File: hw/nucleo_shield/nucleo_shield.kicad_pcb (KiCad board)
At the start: 2 copper layers, 151 x 90.9 mm, 83 parts, among them CN101 Nucleo-F411RE-CN10, CN71 Nucleo-F411RE-CN7, P1 CONN_INH1, P10 CONN_OUTH1, P11 CONN_OUTH2, P12 CONN_RS485_OUT, P13 CONN_RS485_IN, P14 CONN_OUT2, P15 CONN_EXT2, P16 CONN_EXTI2C, P17 CONN_EXT, P18 CONN_1WIRE, P19 CONN_EXT_SPI, P2 CONN_OUT3, P20 CON_BME, P3 CONN_OUT1, P4 POWER_CON, P5 CONN_INH2, P6 ETH_CONN, P7 CONN_LCD_SD, P8 CONN_OUT4, P9 CONN_SCT, U1 74HC595, U10 ULN2803, U11 74HC595, U12 74HC595, U2 74HC595, U3 LTV-847, U4 LTV-847, U5 LTV-847, U6 LTV-847, U7 PCF8574A, U8 PCF8574A, U9 ULN2803

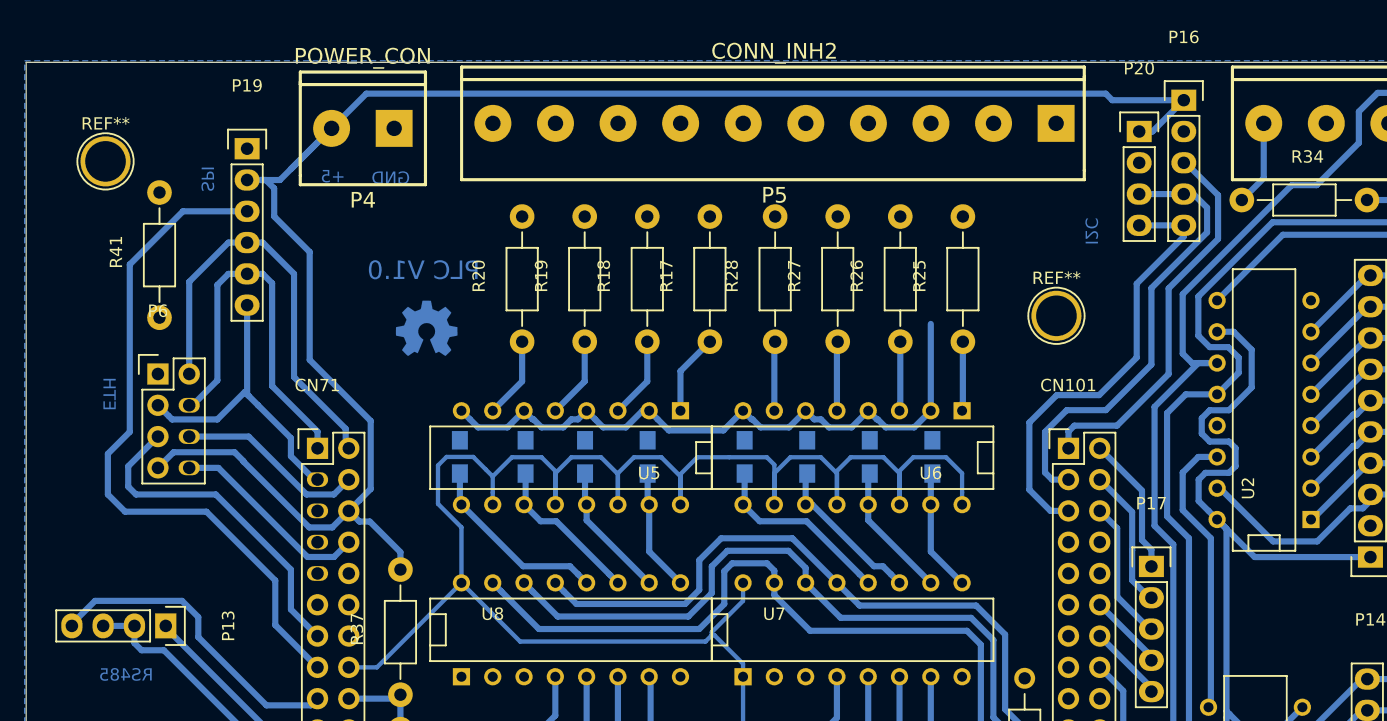
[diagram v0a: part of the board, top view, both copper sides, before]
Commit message: PCB: place connector for BME280
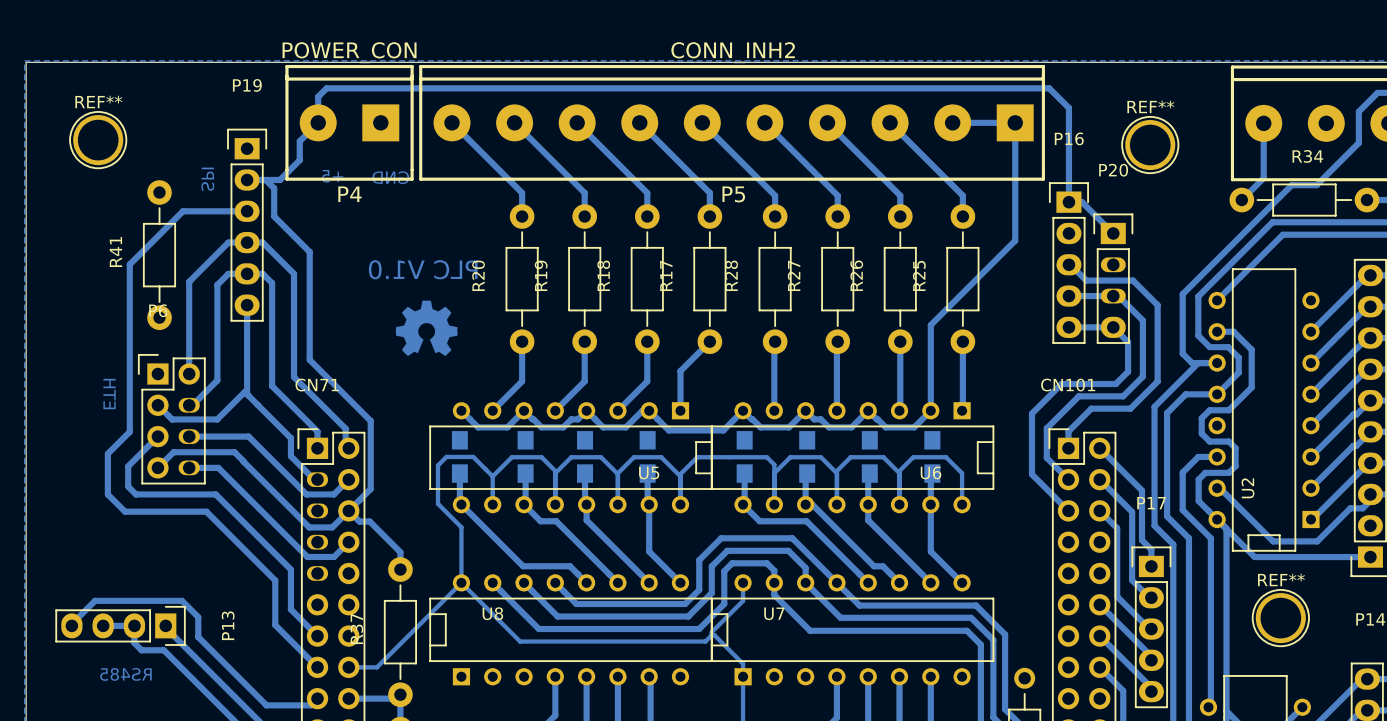
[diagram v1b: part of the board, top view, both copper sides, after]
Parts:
- added REF**: 1pin, Connect:1pin, F.Cu at (197.0, 103.2)
- moved REF** 15.8 mm to (186.4, 64.8)
- moved P16 12.5 mm to (179.8, 69.4)
- moved P20 8.54 mm to (183.4, 71.9)
- moved P5 3.32 mm to (152.5, 63.0)
- moved REF** 1.83 mm to (101.0, 64.4)
- moved P4 1.17 mm to (121.4, 63.0)
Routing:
- net GND_24V: track 129.6 -> 153.8 mm
- net I2C1_SCL: track 37.3 -> 26.2 mm
- net I2C1_SDA: track 36.2 -> 26.1 mm
- net inh16: track 0.00 -> 10.1 mm
- net inh15: track 0.27 -> 10.3 mm
- net inh13: track 0.27 -> 10.3 mm
- net inh14: track 0.00 -> 10.1 mm
- net inh11: track 0.00 -> 9.96 mm
- net inh10: track 0.00 -> 9.96 mm
- net inh9: track 0.04 -> 10.0 mm
- net inh12: track 0.04 -> 10.0 mm
- net I2C_GPIO: track 31.5 -> 25.0 mm
- net +5V: track 536.2 -> 532.6 mm
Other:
- board text removed: "I2C"

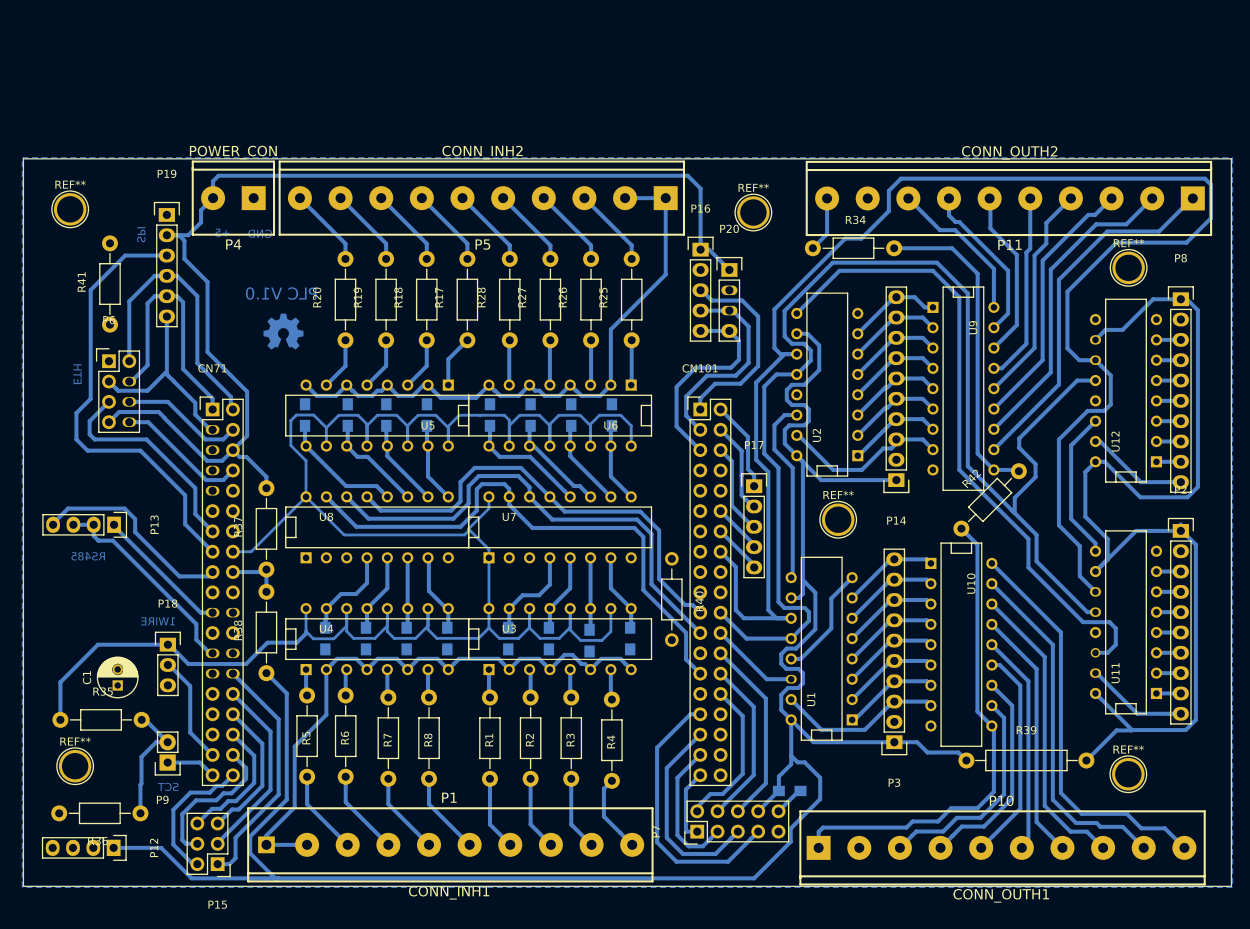
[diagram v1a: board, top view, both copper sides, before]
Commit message: Nucleo: add missing connections
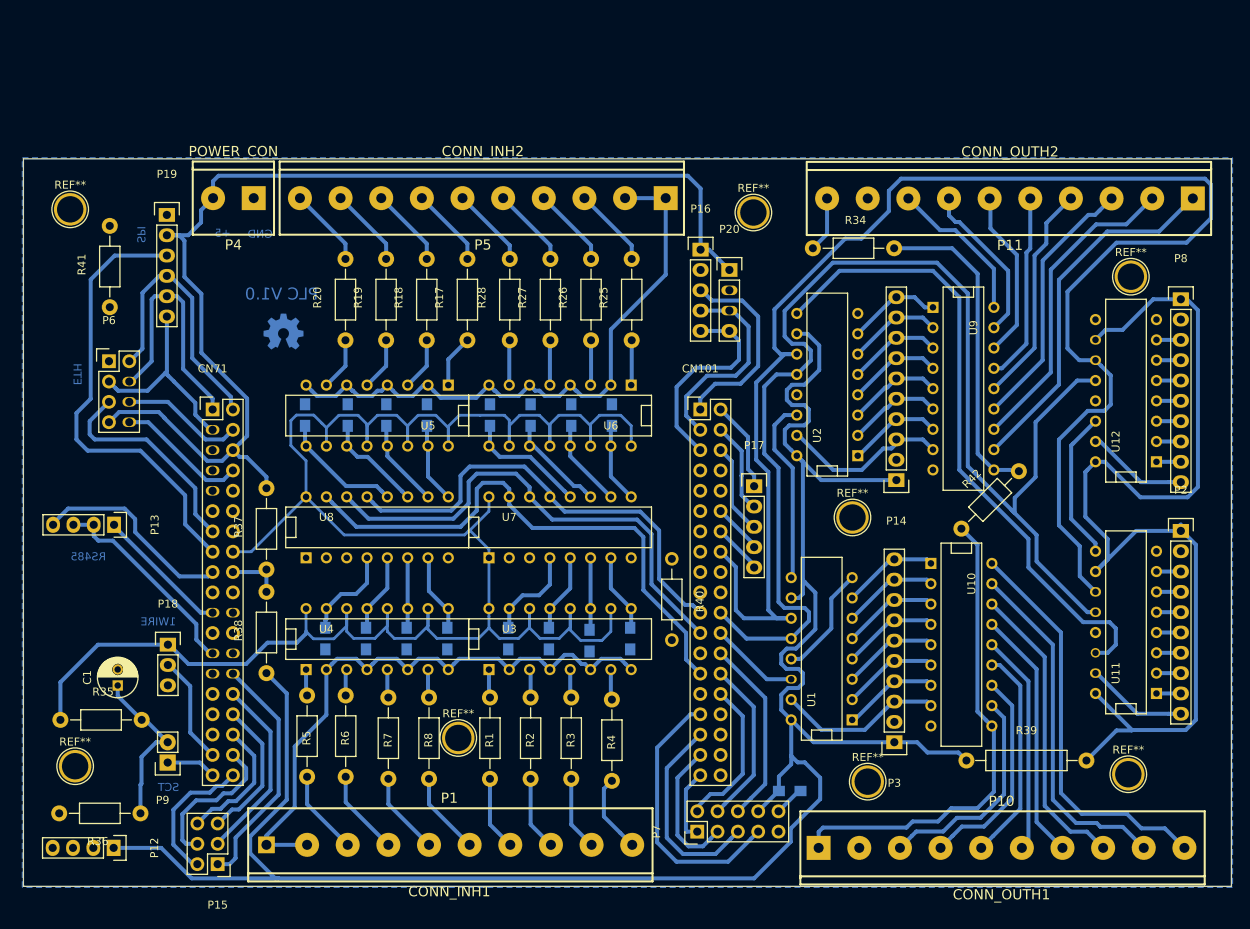
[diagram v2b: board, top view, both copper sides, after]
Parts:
- added REF**: 1pin, Connect:1pin, F.Cu at (198.8, 102.9)
- added REF**: 1pin, Connect:1pin, F.Cu at (149.5, 130.4)
- moved REF** 32.9 mm to (200.7, 135.9)
- moved R41 2.18 mm to (105.9, 71.5)
- moved REF** 1.14 mm to (233.6, 72.8)
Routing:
- net Net-(C1-Pad1): track 15.6 -> 21.1 mm
- net SRLatch: track 160.3 -> 158.6 mm
- net IO_INT: track 57.0 -> 58.0 mm
- net SPI3_MISO: track 34.4 -> 33.6 mm
- net EXT_SPI_SS: track 55.8 -> 56.6 mm
- net I2C3_SCL: track 61.3 -> 61.9 mm

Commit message: Nucleo: update schematic and remove intermediate header for outputs
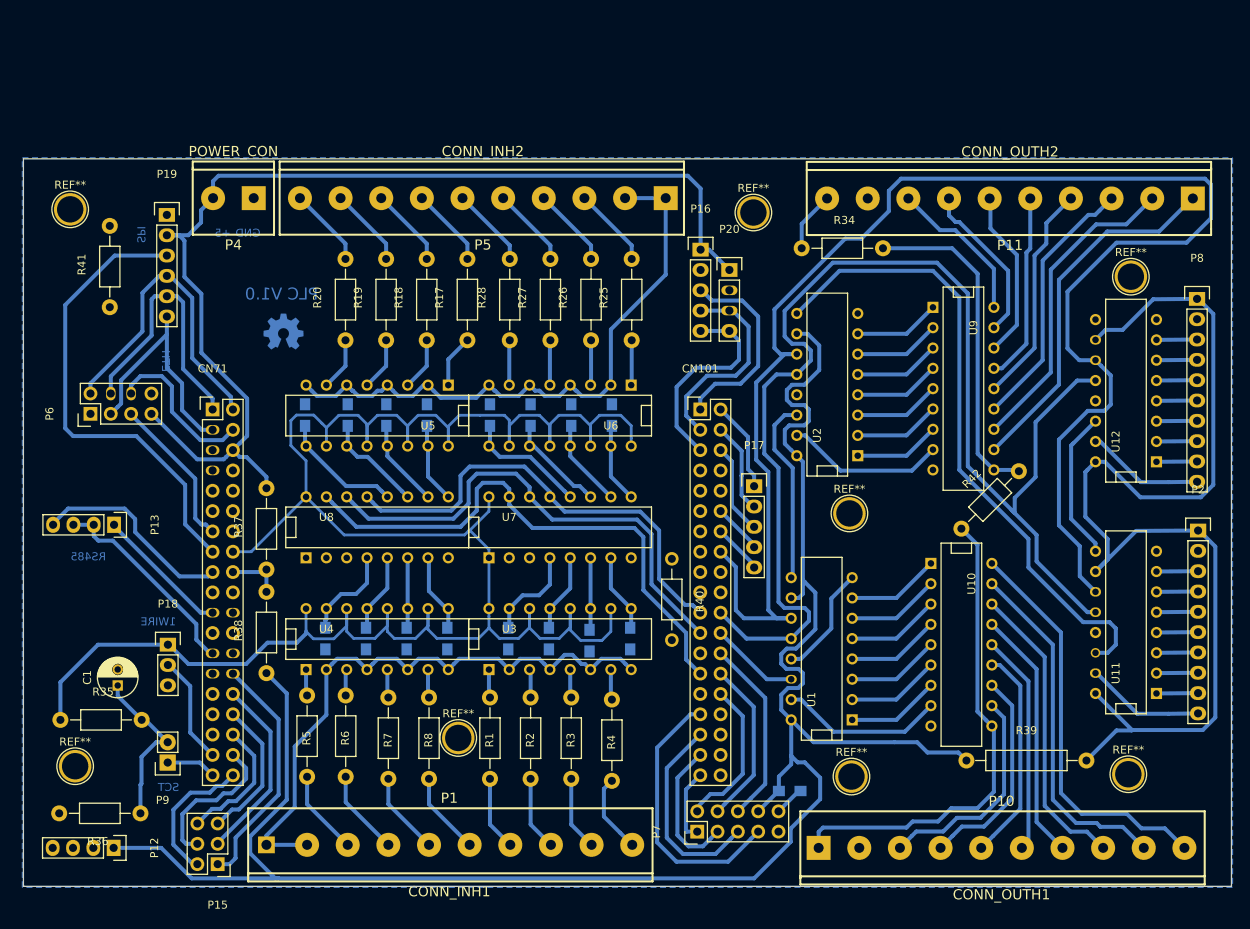
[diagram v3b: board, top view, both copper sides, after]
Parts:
- removed P14: CONN_OUT2, Pin_Headers:Pin_Header_Straight_1x10
- removed P3: CONN_OUT1, Pin_Headers:Pin_Header_Straight_1x10
- moved P6 6.97 mm to (103.5, 89.9), turned to 90 degrees
- moved P2 2.15 mm to (242.0, 104.5)
- moved REF** 2.13 mm to (198.6, 135.3)
- moved P8 2.03 mm to (241.8, 75.5)
- moved R34 1.40 mm to (197.5, 69.2)
- moved REF** 0.64 mm to (198.4, 102.4)
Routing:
- net GND: track 30.7 -> 14.2 mm
- net +5V: track 532.6 -> 520.4 mm
- net ETH_CS: track 27.4 -> 19.2 mm
- net SPI3_MISO: track 33.6 -> 39.6 mm
- net SPI3_MOSI: track 25.7 -> 30.9 mm
- net ETH_RST: track 15.4 -> 19.9 mm
- net SPI3_SCK: track 30.9 -> 33.2 mm
- net out17: track 12.8 -> 14.9 mm
- net out24: track 3.05 -> 5.20 mm
- net out23: track 3.05 -> 5.20 mm
- net out22: track 3.05 -> 5.20 mm
- net out21: track 3.05 -> 5.20 mm
- net out20: track 3.05 -> 5.20 mm
- net out19: track 3.05 -> 5.20 mm
- net out18: track 3.05 -> 5.20 mm
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
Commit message: Nucleo: ad vias
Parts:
- removed G***: LOGO, LOGO
- removed R34, R37, R38, R40, R41, R42: R, Resistors_ThroughHole:Resistor_Horizontal_RM10mm
- removed R39: R, Resistors_ThroughHole:Resistor_Horizontal_RM15mm
- removed the REF** at (198.4, 102.4)
- removed the REF** at (149.5, 130.4)
- removed the REF** at (198.6, 135.3)
- removed the REF** at (186.4, 64.8)
- removed the REF** at (233.6, 72.8)
- removed the REF** at (101.6, 134.0)
- removed the REF** at (233.2, 135.0)
- removed the REF** at (101.0, 64.4)
- added REF**: MountingHole_3mm, Mounting_Holes:MountingHole_3mm, F.Cu at (238.1, 71.8)
- added REF**: MountingHole_3mm, Mounting_Holes:MountingHole_3mm, F.Cu at (238.6, 136.3)
- added REF**: MountingHole_3mm, Mounting_Holes:MountingHole_3mm, F.Cu at (101.9, 64.3)
- added REF**: MountingHole_3mm, Mounting_Holes:MountingHole_3mm, F.Cu at (186.6, 64.5)
- added REF**: MountingHole_3mm, Mounting_Holes:MountingHole_3mm, F.Cu at (200.9, 136.3)
- added REF**: MountingHole_3mm, Mounting_Holes:MountingHole_3mm, F.Cu at (200.4, 102.7)
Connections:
- U9 pad 10: Net-(R34-Pad2) -> +24V
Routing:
- net +24V: track 68.1 -> 123.1 mm, vias 0 -> 4
- net GND: track 14.2 -> 69.1 mm, vias 0 -> 4
- net Net-(R34-Pad2): track 41.7 -> 0.00 mm
- net +5V: track 520.4 -> 555.8 mm, vias 0 -> 6
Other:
- board text removed: "+5"
- board text removed: "1WIRE"
- board text removed: "ETH"
- board text removed: "GND"
- board text removed: "RS485"
- board text removed: "SCT"
- board text removed: "SPI"

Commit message: WIP: add more IO
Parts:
- removed P17: CONN_EXT, Pin_Headers:Pin_Header_Straight_1x05
- removed REF** (x6): MountingHole_3mm, Mounting_Holes:MountingHole_3mm
- added P3: POWER_24V_CON, w_conn_screw:mors_2p, F.Cu at (112.9, 62.7)
- added U14: PCF8574A, Housings_DIP:DIP-16__300, F.Cu at (193.8, 97.9)
- P1, P10, P11, P5: footprint w_conn_screw:mors_10p -> w_conn_screw:mors_8p
- P2, P8: footprint Pin_Headers:Pin_Header_Straight_1x10 -> Pin_Headers:Pin_Header_Straight_1x08
- moved U2 57.2 mm to (235.8, 126.9)
- moved P16 49.2 mm to (225.7, 51.7), turned to 180 degrees
- moved P20 44.3 mm to (221.4, 49.1), turned to 180 degrees
- moved U11 33.9 mm to (220.0, 84.7), turned to 180 degrees
- moved P19 23.7 mm to (100.3, 85.1), turned to 90 degrees
- moved U1 22.9 mm to (217.6, 122.7), turned to 0 degrees
- moved P4 19.9 mm to (101.5, 62.7)
- moved R20 15.8 mm to (119.6, 75.1)
- moved R25 15.8 mm to (155.4, 80.3)
- moved R19 15.8 mm to (124.7, 75.3)
- moved R17 15.8 mm to (134.9, 75.3)
- moved R18 15.8 mm to (129.8, 75.3)
- moved R26 15.8 mm to (150.3, 80.3)
- moved R27 15.8 mm to (145.2, 80.3)
- moved R28 15.8 mm to (140.2, 80.3)
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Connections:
- CN101 pad 10: (no net) -> Net-(CN101-Pad10)
- CN101 pad 11: (no net) -> Net-(CN101-Pad11)
- CN101 pad 12: Net-(CN101-Pad12) -> SRLatch2
- CN101 pad 13: (no net) -> Net-(CN101-Pad13)
- CN101 pad 14: Net-(CN101-Pad14) -> SRDATA2
- CN101 pad 15: (no net) -> Net-(CN101-Pad15)
- CN101 pad 17: (no net) -> Net-(CN101-Pad17)
- CN101 pad 18: (no net) -> Net-(CN101-Pad18)
- CN101 pad 19: (no net) -> Net-(CN101-Pad19)
- CN101 pad 2: Net-(CN101-Pad2) -> I2C1_GPIO
- CN101 pad 25: (no net) -> Net-(CN101-Pad25)
- CN101 pad 29: (no net) -> Net-(CN101-Pad29)
- CN101 pad 32: (no net) -> Net-(CN101-Pad32)
- CN101 pad 34: (no net) -> Net-(CN101-Pad34)
- CN101 pad 36: (no net) -> Net-(CN101-Pad36)
- CN101 pad 38: (no net) -> Net-(CN101-Pad38)
- CN101 pad 6: Net-(CN101-Pad6) -> SRCLK2
- CN101 pad 7: (no net) -> Net-(CN101-Pad7)
- CN101 pad 8: (no net) -> Net-(CN101-Pad8)
- CN71 pad 10: (no net) -> Net-(CN71-Pad10)
- CN71 pad 11: (no net) -> Net-(CN71-Pad11)
- CN71 pad 12: (no net) -> Net-(CN71-Pad12)
- CN71 pad 14: (no net) -> Net-(CN71-Pad14)
- CN71 pad 23: (no net) -> Net-(CN71-Pad23)
- CN71 pad 24: (no net) -> Net-(CN71-Pad24)
- CN71 pad 26: (no net) -> Net-(CN71-Pad26)
- CN71 pad 27: (no net) -> Net-(CN71-Pad27)
- CN71 pad 29: (no net) -> Net-(CN71-Pad29)
- CN71 pad 31: (no net) -> Net-(CN71-Pad31)
- CN71 pad 33: (no net) -> Net-(CN71-Pad33)
- CN71 pad 7: (no net) -> Net-(CN71-Pad7)
- CN71 pad 9: (no net) -> Net-(CN71-Pad9)
- P1 pad 1: GND_24V -> inh5
- P1 pad 2: GND_24V -> inh6
- P1 pad 3: inh5 -> inh7
- P1 pad 4: inh6 -> inh8
- P1 pad 5: inh7 -> inh1
- P1 pad 6: inh8 -> inh2
- P1 pad 7: inh1 -> inh3
- P1 pad 8: inh2 -> inh4
- P10 pad 1: +24V -> out1h
- P10 pad 2: GND -> out2h
- P10 pad 3: out1h -> out3h
- P10 pad 4: out2h -> out4h
- P10 pad 5: out3h -> out5h
- P10 pad 6: out4h -> out6h
- P10 pad 7: out5h -> out7h
- P10 pad 8: out6h -> out8h
- P12 pad 2: (no net) -> Net-(P12-Pad2)
- P12 pad 3: (no net) -> Net-(P12-Pad3)
- P2 pad 1: +5V -> out24
- P2 pad 2: GND -> out23
- P2 pad 3: out24 -> out22
- P2 pad 4: out23 -> out21
- P2 pad 5: out22 -> out20
- P2 pad 6: out21 -> out19
- P2 pad 7: out20 -> out18
- P2 pad 8: out19 -> out17
- P5 pad 1: GND_24V -> inh16
- P5 pad 2: GND_24V -> inh15
- P5 pad 3: inh16 -> inh14
- P5 pad 4: inh15 -> inh13
- P5 pad 5: inh14 -> inh11
- P5 pad 6: inh13 -> inh12
- P5 pad 7: inh11 -> inh10
- P5 pad 8: inh12 -> inh9
- P8 pad 1: +5V -> out32
- P8 pad 2: GND -> out31
- P8 pad 3: out32 -> out30
- P8 pad 4: out31 -> out29
- P8 pad 5: out30 -> out28
- P8 pad 6: out29 -> out27
- P8 pad 7: out28 -> out26
- P8 pad 8: out27 -> out25
- U11 pad 1: out18 -> out10
- U11 pad 11: SRCLK -> SRLatch2
- U11 pad 12: SRLatch -> SRCLK2
- U11 pad 14: Net-(U11-Pad14) -> SRDATA2
- U11 pad 15: out17 -> out9
- U11 pad 2: out19 -> out11
- U11 pad 3: out20 -> out12
- U11 pad 4: out21 -> out13
- U11 pad 5: out22 -> out14
- U11 pad 6: out23 -> out15
- U11 pad 7: out24 -> out16
- U12 pad 11: SRCLK -> SRLatch2
- U12 pad 12: SRLatch -> SRCLK2
- U12 pad 9: (no net) -> Net-(U12-Pad9)
- U2 pad 1: out10 -> out18
- U2 pad 11: SRCLK -> Net-(U2-Pad11)
- U2 pad 12: SRLatch -> Net-(U2-Pad12)
- U2 pad 15: out9 -> out17
- U2 pad 2: out11 -> out19
- U2 pad 3: out12 -> out20
- U2 pad 4: out13 -> out21
- U2 pad 5: out14 -> out22
- U2 pad 6: out15 -> out23
- U2 pad 7: out16 -> out24
- U2 pad 9: Net-(U11-Pad14) -> Net-(U2-Pad9)
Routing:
- net +5V: track 555.8 -> 92.0 mm, vias 6 -> 4
- net SRCLK: track 198.6 -> 0.00 mm
- net SRLatch: track 158.6 -> 0.00 mm
- net +24V: track 123.1 -> 0.00 mm, vias 4 -> 0
- net Net-(U11-Pad14): track 80.3 -> 0.00 mm
- net GND_24V: track 153.8 -> 92.5 mm
- net EXT_SPI_SS: track 58.5 -> 0.00 mm
- net out8h: track 50.6 -> 0.00 mm
- net GND: track 69.1 -> 20.3 mm, vias 4 -> 2
- net out9h: track 45.5 -> 0.00 mm
- net out7h: track 44.0 -> 0.00 mm
- net out10h: track 39.3 -> 0.00 mm
- net SPI3_MISO: track 39.6 -> 0.36 mm
- net out6h: track 37.4 -> 0.00 mm
- net SD_CS: track 34.2 -> 0.00 mm
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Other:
- board text removed: "PLC V1.0"
